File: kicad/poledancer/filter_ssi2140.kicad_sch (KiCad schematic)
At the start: 92 parts, among them U10 AS3364, U11 TL074, U12 SSI2140, U13 SSI2190, U14 TL074, U15 DG442xY, U3 TL074

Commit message: placement looks ok.  Some tweakin, yes, but call it workable.
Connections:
- net VCF_LOWPASS_OUT: now also U3.7; no longer U3.1
- net VCF_MIXED_OUT: now also U3.1; no longer U3.7
- net at R76.1, R77.2: now also U3.6 (-); no longer U3.2 (-)
- net at C44.2, R79.2, U13.12 (MIX): now also U3.2 (-); no longer U3.6 (-)
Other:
- moved on the sheet: U3A, U3B
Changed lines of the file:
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@@
   (junction (at 77.47 53.34) (diameter 0) (color 0 0 0 0)
   )
-  (junction (at 350.52 125.73) (diameter 0) (color 0 0 0 0)
-  )
   (junction (at 400.05 64.77) (diameter 0) (color 0 0 0 0)
   )
@@
   (junction (at 170.18 76.2) (diameter 0) (color 0 0 0 0)
   )
+  (junction (at 349.885 125.73) (diameter 0) (color 0 0 0 0)
+  )
   (junction (at 279.4 138.43) (diameter 0) (color 0 0 0 0)
   )
@@
     (stroke (width 0) (type default))
   )
+  (wire (pts (xy 349.885 125.73) (xy 350.52 125.73))
+    (stroke (width 0) (type default))
+  )
   (wire (pts (xy 212.09 246.38) (xy 213.36 246.38))
     (stroke (width 0) (type default))
@@
     (stroke (width 0) (type default))
   )
-  (wire (pts (xy 350.52 125.73) (xy 350.52 119.38))
+  (wire (pts (xy 349.885 125.73) (xy 349.885 119.38))
     (stroke (width 0) (type default))
   )
@@
     (stroke (width 0) (type default))
   )
-  (wire (pts (xy 347.98 125.73) (xy 350.52 125.73))
+  (wire (pts (xy 347.98 125.73) (xy 349.885 125.73))
     (stroke (width 0) (type default))
   )
@@
     (stroke (width 0) (type default))
   )
-  (wire (pts (xy 350.52 119.38) (xy 354.33 119.38))
+  (wire (pts (xy 349.885 119.38) (xy 354.33 119.38))
     (stroke (width 0) (type default))
   )
@@
     )
   )
-  (symbol (lib_id "Amplifier_Operational:TL074") (at 358.14 128.27 0) (mirror x) (unit 1)
+  (symbol (lib_id "Amplifier_Operational:TL074") (at 368.3 167.64 0) (mirror x) (unit 1)
     (in_bom yes) (on_board yes) (dnp no)
-    (property "Reference" "U3" (at 359.41 123.19 0)
+    (property "Reference" "U3" (at 369.57 162.56 0)
       (effects (font (size 1.27 1.27)))
     )
-    (property "Value" "TL074" (at 358.14 128.27 0)
+    (property "Value" "TL074" (at 368.3 167.64 0)
       (effects (font (size 1.27 1.27)))
     )
-    (property "Footprint" "Package_SO:TSSOP-14_4.4x5mm_P0.65mm" (at 356.87 130.81 0)
+    (property "Footprint" "Package_SO:TSSOP-14_4.4x5mm_P0.65mm" (at 367.03 170.18 0)
       (effects (font (size 1.27 1.27)) hide)
     )
-    (property "Datasheet" "http://www.ti.com/lit/ds/symlink/tl071.pdf" (at 359.41 133.35 0)
+    (property "Datasheet" "http://www.ti.com/lit/ds/symlink/tl071.pdf" (at 369.57 172.72 0)
       (effects (font (size 1.27 1.27)) hide)
     )
-    (property "LCSC" "C96507" (at 358.14 128.27 0)
+    (property "LCSC" "C96507" (at 368.3 167.64 0)
       (effects (font (size 1.27 1.27)) hide)
     )
@@
     )
   )
-  (symbol (lib_id "Amplifier_Operational:TL074") (at 368.3 167.64 0) (mirror x) (unit 2)
+  (symbol (lib_id "Amplifier_Operational:TL074") (at 358.14 128.27 0) (mirror x) (unit 2)
     (in_bom yes) (on_board yes) (dnp no)
-    (property "Reference" "U3" (at 369.57 162.56 0)
+    (property "Reference" "U3" (at 359.41 123.19 0)
       (effects (font (size 1.27 1.27)))
     )
-    (property "Value" "TL074" (at 367.03 167.64 0)
+    (property "Value" "TL074" (at 356.87 128.27 0)
       (effects (font (size 1.27 1.27)))
     )
-    (property "Footprint" "Package_SO:TSSOP-14_4.4x5mm_P0.65mm" (at 367.03 170.18 0)
+    (property "Footprint" "Package_SO:TSSOP-14_4.4x5mm_P0.65mm" (at 356.87 130.81 0)
       (effects (font (size 1.27 1.27)) hide)
     )
-    (property "Datasheet" "http://www.ti.com/lit/ds/symlink/tl071.pdf" (at 369.57 172.72 0)
+    (property "Datasheet" "http://www.ti.com/lit/ds/symlink/tl071.pdf" (at 359.41 133.35 0)
       (effects (font (size 1.27 1.27)) hide)
     )
-    (property "LCSC" "C96507" (at 368.3 77.47 0)
+    (property "LCSC" "C96507" (at 358.14 38.1 0)
       (effects (font (size 1.27 1.27)) hide)
     )

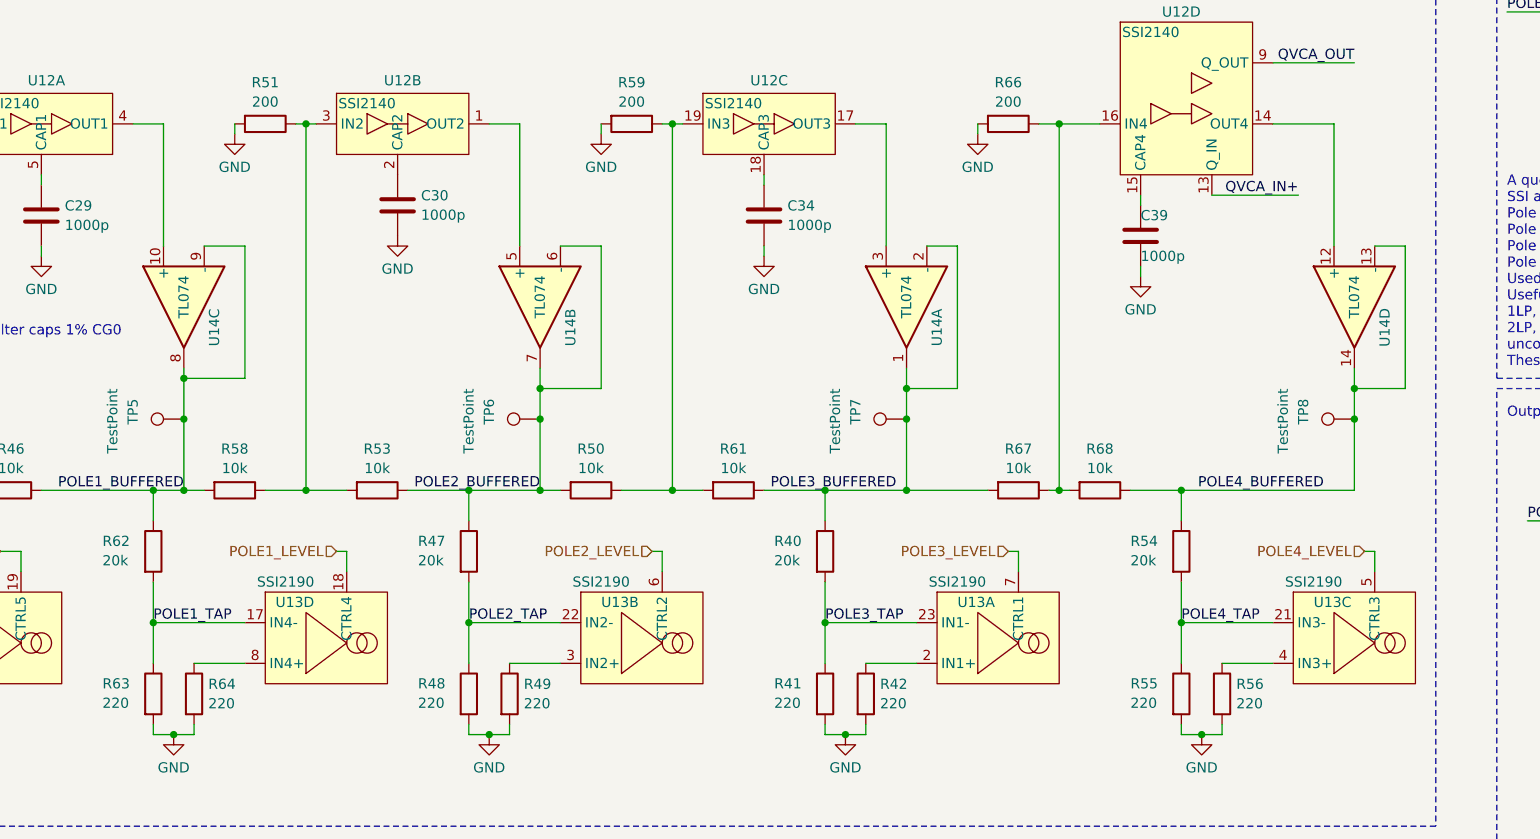
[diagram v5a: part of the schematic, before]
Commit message: swap some instances around for better routing
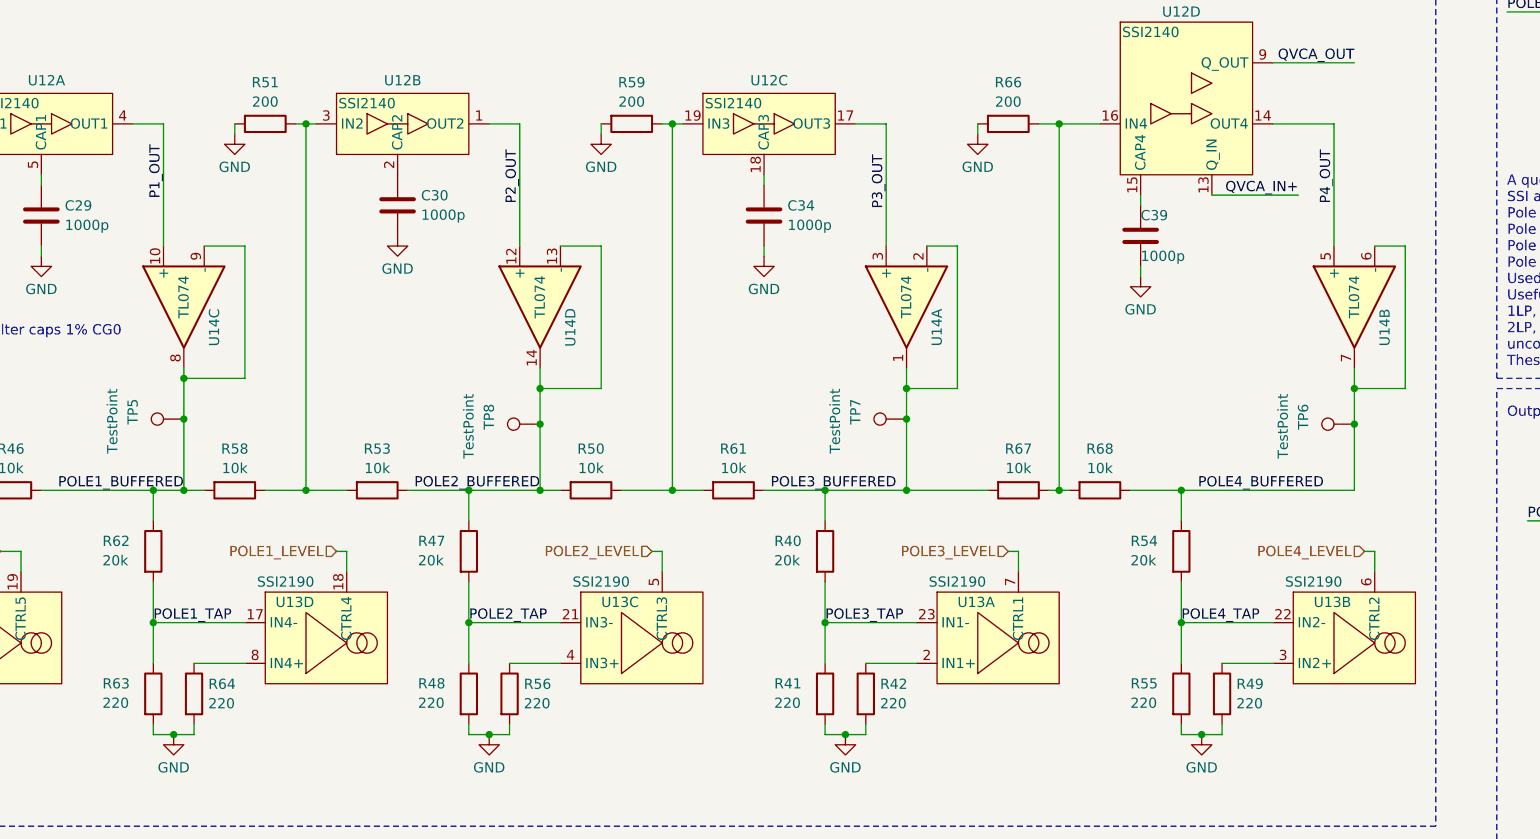
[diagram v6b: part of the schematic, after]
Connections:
- net POLE2_BUFFERED: now also TP8.1, U14.13 (-), U14.14; no longer TP6.1, U14.6 (-), U14.7
- net POLE2_LEVEL: now also U13.5 (CTRL3); no longer U13.6 (CTRL2)
- net POLE2_TAP: now also U13.21 (IN3-); no longer U13.22 (IN2-)
- net POLE4_BUFFERED: now also TP6.1, U14.6 (-), U14.7; no longer TP8.1, U14.13 (-), U14.14
- net POLE4_LEVEL: now also U13.6 (CTRL2); no longer U13.5 (CTRL3)
- net POLE4_TAP: now also U13.22 (IN2-); no longer U13.21 (IN3-)
- net P2_OUT: now reaches U12.1 (OUT2)
- net P2_OUT: now also U14.12 (+); no longer U14.5 (+)
- net P1_OUT: now reaches U12.4 (OUT1), U14.10 (+)
- net P3_OUT: now reaches U12.17 (OUT3), U14.3 (+)
- net P4_OUT: now reaches U12.14 (OUT4)
- net P4_OUT: now also U14.5 (+); no longer U14.12 (+)
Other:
- moved on the sheet: R49, R56, TP6, TP8, U13B, U13C, U14B, U14D

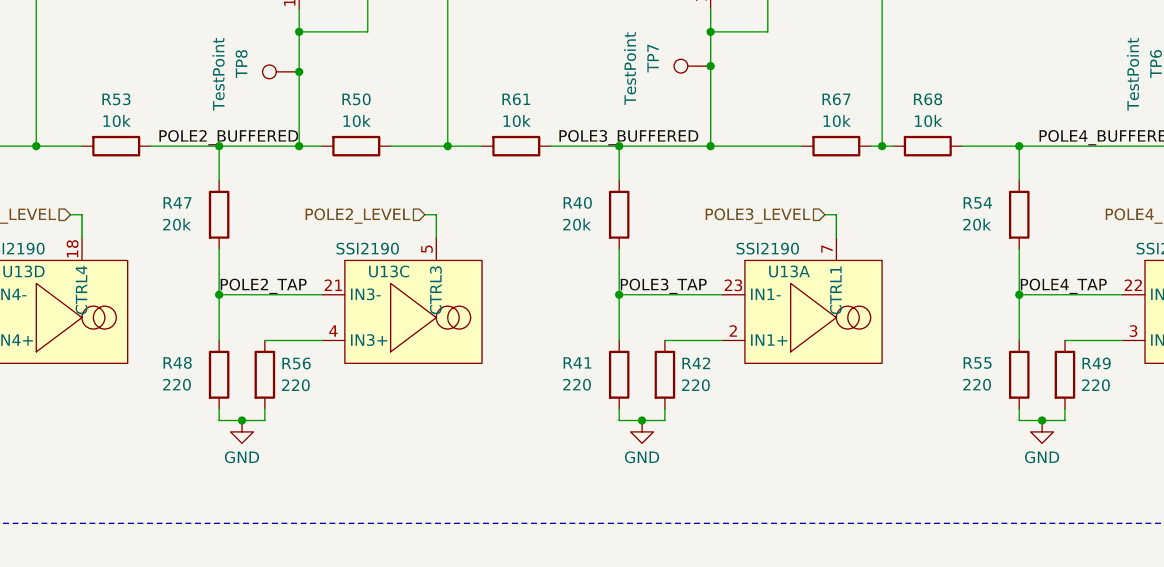
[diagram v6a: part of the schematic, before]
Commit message: start routing power
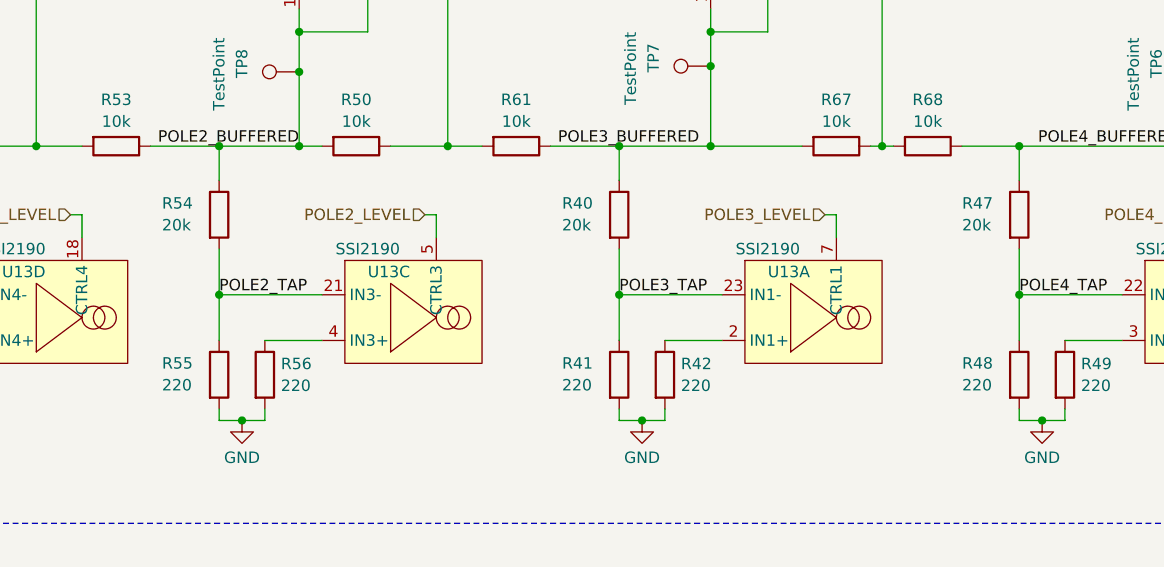
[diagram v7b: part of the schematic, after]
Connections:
- net POLE2_BUFFERED: now also R54.1; no longer R47.1
- net POLE2_TAP: now also R54.2, R55.1; no longer R47.2, R48.1
- net POLE4_BUFFERED: now also R47.1; no longer R54.1
- net POLE4_TAP: now also R47.2, R48.1; no longer R54.2, R55.1
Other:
- moved on the sheet: R47, R48, R54, R55
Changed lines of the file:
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@@
     )
   )
-  (symbol (lib_id "Device:R") (at 279.4 147.32 0) (unit 1)
+  (symbol (lib_id "Device:R") (at 190.5 147.32 0) (unit 1)
     (in_bom yes) (on_board yes) (dnp no)
-    (property "Reference" "R55" (at 273.05 146.05 0)
+    (property "Reference" "R55" (at 184.15 146.05 0)
       (effects (font (size 1.27 1.27)) (justify left))
     )
-    (property "Value" "220" (at 273.05 148.4742 0)
+    (property "Value" "220" (at 184.15 148.4742 0)
       (effects (font (size 1.27 1.27)) (justify left))
     )
-    (property "Footprint" "Resistor_SMD:R_0603_1608Metric" (at 277.622 147.32 90)
+    (property "Footprint" "Resistor_SMD:R_0603_1608Metric" (at 188.722 147.32 90)
       (effects (font (size 1.27 1.27)) hide)
     )
-    (property "Datasheet" "~" (at 279.4 147.32 0)
+    (property "Datasheet" "~" (at 190.5 147.32 0)
       (effects (font (size 1.27 1.27)) hide)
     )
-    (property "LCSC" "C22962" (at 279.4 147.32 0)
+    (property "LCSC" "C22962" (at 190.5 147.32 0)
       (effects (font (size 1.27 1.27)) hide)
     )
@@
     )
   )
-  (symbol (lib_id "Device:R") (at 190.5 129.54 0) (unit 1)
+  (symbol (lib_id "Device:R") (at 279.4 129.54 0) (unit 1)
     (in_bom yes) (on_board yes) (dnp no)
-    (property "Reference" "R47" (at 184.15 128.27 0)
+    (property "Reference" "R47" (at 273.05 128.27 0)
       (effects (font (size 1.27 1.27)) (justify left))
     )
-    (property "Value" "20k" (at 184.15 130.6942 0)
+    (property "Value" "20k" (at 273.05 130.6942 0)
       (effects (font (size 1.27 1.27)) (justify left))
     )
-    (property "Footprint" "Resistor_SMD:R_0603_1608Metric" (at 188.722 129.54 90)
+    (property "Footprint" "Resistor_SMD:R_0603_1608Metric" (at 277.622 129.54 90)
       (effects (font (size 1.27 1.27)) hide)
     )
-    (property "Datasheet" "~" (at 190.5 129.54 0)
+    (property "Datasheet" "~" (at 279.4 129.54 0)
       (effects (font (size 1.27 1.27)) hide)
     )
-    (property "LCSC" "C4184" (at 190.5 129.54 0)
+    (property "LCSC" "C4184" (at 279.4 129.54 0)
       (effects (font (size 1.27 1.27)) hide)
     )
@@
     )
   )
-  (symbol (lib_id "Device:R") (at 190.5 147.32 0) (unit 1)
+  (symbol (lib_id "Device:R") (at 279.4 147.32 0) (unit 1)
     (in_bom yes) (on_board yes) (dnp no)
-    (property "Reference" "R48" (at 184.15 146.05 0)
+    (property "Reference" "R48" (at 273.05 146.05 0)
       (effects (font (size 1.27 1.27)) (justify left))
     )
-    (property "Value" "220" (at 184.15 148.4742 0)
+    (property "Value" "220" (at 273.05 148.4742 0)
       (effects (font (size 1.27 1.27)) (justify left))
     )
-    (property "Footprint" "Resistor_SMD:R_0603_1608Metric" (at 188.722 147.32 90)
+    (property "Footprint" "Resistor_SMD:R_0603_1608Metric" (at 277.622 147.32 90)
       (effects (font (size 1.27 1.27)) hide)
     )
-    (property "Datasheet" "~" (at 190.5 147.32 0)
+    (property "Datasheet" "~" (at 279.4 147.32 0)
       (effects (font (size 1.27 1.27)) hide)
     )
-    (property "LCSC" "C22962" (at 190.5 147.32 0)
+    (property "LCSC" "C22962" (at 279.4 147.32 0)
       (effects (font (size 1.27 1.27)) hide)
     )
@@
     )
   )
-  (symbol (lib_id "Device:R") (at 279.4 129.54 0) (unit 1)
+  (symbol (lib_id "Device:R") (at 190.5 129.54 0) (unit 1)
     (in_bom yes) (on_board yes) (dnp no)
-    (property "Reference" "R54" (at 273.05 128.27 0)
+    (property "Reference" "R54" (at 184.15 128.27 0)
       (effects (font (size 1.27 1.27)) (justify left))
     )
-    (property "Value" "20k" (at 273.05 130.6942 0)
+    (property "Value" "20k" (at 184.15 130.6942 0)
       (effects (font (size 1.27 1.27)) (justify left))
     )
-    (property "Footprint" "Resistor_SMD:R_0603_1608Metric" (at 277.622 129.54 90)
+    (property "Footprint" "Resistor_SMD:R_0603_1608Metric" (at 188.722 129.54 90)
       (effects (font (size 1.27 1.27)) hide)
     )
-    (property "Datasheet" "~" (at 279.4 129.54 0)
+    (property "Datasheet" "~" (at 190.5 129.54 0)
       (effects (font (size 1.27 1.27)) hide)
     )
-    (property "LCSC" "C4184" (at 279.4 129.54 0)
+    (property "LCSC" "C4184" (at 190.5 129.54 0)
       (effects (font (size 1.27 1.27)) hide)
     )

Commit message: geo reannotate
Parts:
- renumbered C42 to C1, C35 to C11, C32 to C12, C31 to C13, C30 to C14, C40 to C15, C29 to C16, C34 to C17, C39 to C18, C26 to C19, C43 to C2, C36 to C20, C41 to C24, C37 to C3, C44 to C30, C33 to C32, C25 to C34, C28 to C36, C38 to C4, C27 to C5, R40 to R1, R68 to R10, R67 to R11, R29 to R12, R33 to R18, R62 to R19, R47 to R2, R63 to R20, R55 to R21, R64 to R22, R37 to R23, R69 to R24, R31 to R25, R70 to R26, R81 to R27, R54 to R28, R57 to R29, R48 to R3, R56 to R30, R80 to R31, R71 to R32, R73 to R33, R53 to R34, R44 to R35, R43 to R36, R50 to R37, R28 to R38, R61 to R39, R88 to R4, R45 to R40, R85 to R41, R58 to R42, R39 to R43, R87 to R44, R86 to R45, R59 to R46, R51 to R47, R75 to R49, R49 to R5, R74 to R56, R76 to R59, R66 to R6, R32 to R60, R34 to R61, R79 to R66, R77 to R67, R38 to R68, R36 to R69, R41 to R7, R26 to R70, R35 to R71, R27 to R72, R42 to R8, R46 to R9, TP2 to TP10, TP4 to TP11, TP5 to TP2, TP6 to TP3, TP8 to TP4, TP7 to TP5, TP3 to TP6, TP10 to TP7, U14 to U1, U3 to U10, U13 to U2, U10 to U3, U11 to U4, U12 to U5, U15 to U7
